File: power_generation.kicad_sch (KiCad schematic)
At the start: 0 parts

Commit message: Add 5V and 3.3V power generation
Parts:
- added C301, C307: 10 µF, Capacitor_SMD:C_0603_1608Metric, symbol Device:C
- added C302, C308: 0.1 µF, perfect_footprints:C_0402_1005Metric, symbol Device:C
- added C303: 3300 pF, symbol Device:C
- added C304, C305, C306, C310, C311, C312: 22 µF, symbol Device:C
- added C309: 3600 pF, symbol Device:C
- added D301, D302: 150060RS75000, LED_SMD:LED_0603_1608Metric, symbol Device:LED
- added J301, J302: 61300211121, Connector_PinHeader_2.54mm:PinHeader_2x01_P2.54mm_Vertical, symbol Connector_Generic:Conn_01x02
- added L301: 3.3 µH, symbol Device:L
- added L302: 2.7 µH, symbol Device:L
- added R301: 127 kΩ, perfect_footprints:R_0402_1005Metric, symbol Device:R
- added R302: 24 kΩ, perfect_footprints:R_0402_1005Metric, symbol Device:R
- added R303: 34.8 kΩ, perfect_footprints:R_0402_1005Metric, symbol Device:R
- added R304, R305: 100 kΩ, perfect_footprints:R_0402_1005Metric, symbol Device:R
- added R306: 23.7 kΩ, perfect_footprints:R_0402_1005Metric, symbol Device:R
- added R307: 215 kΩ, perfect_footprints:R_0402_1005Metric, symbol Device:R
- added R308: 68 kΩ, perfect_footprints:R_0402_1005Metric, symbol Device:R
- added R309: 1 kΩ, perfect_footprints:R_0402_1005Metric, symbol Device:R
- added R310, R311: 0 Ω, Resistor_SMD:R_0805_2012Metric, symbol Device:R
- added R312: 330 Ω, perfect_footprints:R_0402_1005Metric, symbol Device:R
- added U301, U302: AP64500SP-13, Package_SO:Diodes_SO-8EP, symbol Diodes Incorporated:AP64500
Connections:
- net V_3V3: now also C310.1, C311.1, C312.1, J302.1 (Pin_1), L302.2, R307.1, R311.2
- net V_5V0: now also C304.1, C305.1, C306.1, J301.1 (Pin_1), L301.2, R301.1, R310.2
- net V_SYS: now also C301.1, C307.1, U301.2 (VIN), U301.3 (EN), U302.2 (VIN), U302.3 (EN)
- new net: J301.2 (Pin_2), R309.1, R310.1
- new net: C309.1, R306.2
- new net: D301.2 (A), R309.2
- new net: J302.2 (Pin_2), R311.1, R312.1
- new net: C303.1, R303.2
- new net: D302.2 (A), R312.2
- new net BST_V_3V3: C308.1, U302.1 (BST)
- new net BST_V_5V0: C302.1, U301.1 (BST)
- new net COMP_V_3V3: R306.1, U302.6 (COMP)
- new net COMP_V_5V0: R303.1, U301.6 (COMP)
- new net FB_V_3V3: R307.2, R308.1, U302.5 (FB)
- new net FB_V_5V0: R301.2, R302.1, U301.5 (FB)
- new net GND: C301.2, C303.2, C304.2, C305.2, C306.2, C307.2, C309.2, C310.2, C311.2, C312.2, D301.1 (K), D302.1 (K), R302.2, R304.2, R305.2, R308.2, U301.7 (GND), U302.7 (GND)
- new net RT_V_3V3: R305.1, U302.4 (RT/CLK)
- new net RT_V_5V0: R304.1, U301.4 (RT/CLK)
- new net SW_V_3V3: C308.2, L302.1, U302.8 (SW)
- new net SW_V_5V0: C302.2, L301.1, U301.8 (SW)
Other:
- note added: "C_{COMP}"
- note added: "R_{COMP}"
- note added: "R_{FBB}"
- note added: "R_{FBT}"
- note added: "R_{RT}"

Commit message: Add MPU power generation
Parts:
- added TP301, TP302: TestPoint, TestPoint:TestPoint_Pad_D1.0mm, symbol Connector:TestPoint
- U301: MPN (none) -> AP64500SP-13; Manufacturer Part Number AP64500SP-13 -> (none)
- U302: MPN (none) -> AP64500SP-13
- renumbered C307 to C302, C302 to C303, C303 to C304, C308 to C305, C309 to C306, C304 to C307, C310 to C308, C305 to C309, C311 to C310, C306 to C311, R304 to R301, R305 to R302, R306 to R304, R301 to R305, R302 to R306, R310 to R309, R309 to R310
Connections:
- net V_3V3: now also TP302.1
- net V_5V0: now also TP301.1
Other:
- added sheet Power generation MPU (power_generation_mpu.kicad_sch)

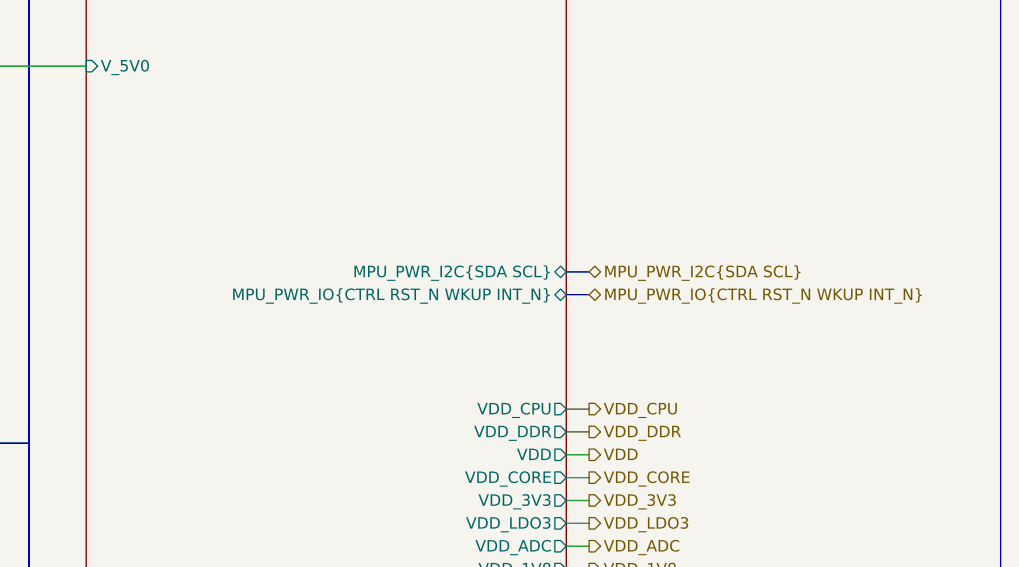
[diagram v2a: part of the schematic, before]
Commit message: Reorganize schema and add MPU
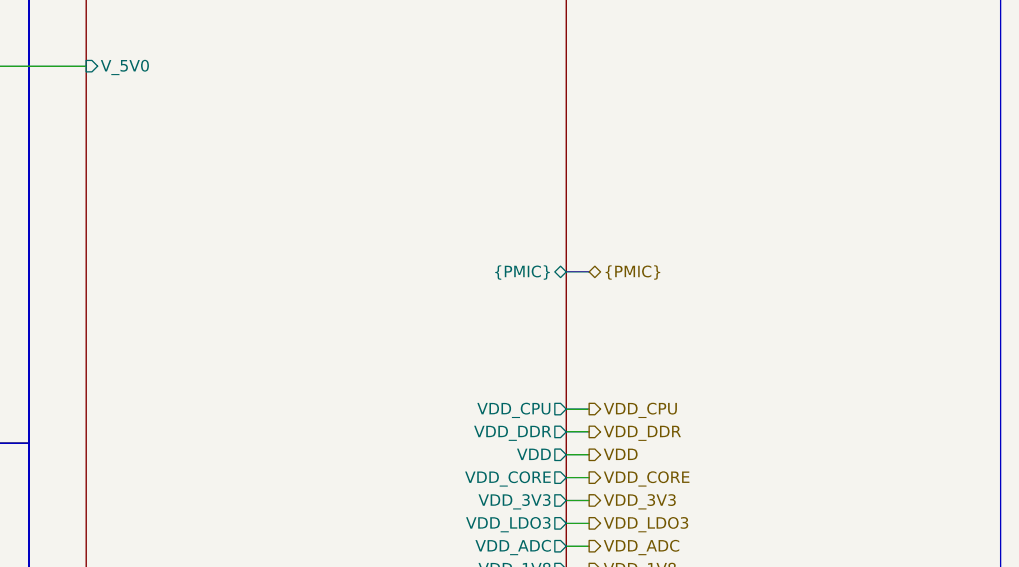
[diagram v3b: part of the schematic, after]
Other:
- sheet Power generation MPU ports: added {PMIC}; removed MPU_PWR_I2C{SDA SCL}, MPU_PWR_IO{CTRL RST_N WKUP INT_N}
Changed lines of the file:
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@@
 		)
 	)
-	(bus
-		(pts
-			(xy 358.14 129.54) (xy 360.68 129.54)
-		)
-		(stroke
-			(width 0)
-			(type default)
-		)
-	)
 	(wire
 		(pts
@@
 		)
 	)
-	(hierarchical_label "MPU_PWR_IO{CTRL RST_N WKUP INT_N}"
-		(shape bidirectional)
-		(at 360.68 129.54 0)
-		(effects
-			(font
-				(size 1.27 1.27)
-			)
-			(justify left)
-		)
-	)
 	(hierarchical_label "VDD_3V3"
 		(shape output)
@@
 		)
 	)
-	(hierarchical_label "MPU_PWR_I2C{SDA SCL}"
+	(hierarchical_label "{PMIC}"
 		(shape bidirectional)
 		(at 360.68 127 0)
@@
 			)
 		)
-		(pin "MPU_PWR_I2C{SDA SCL}" bidirectional
+		(pin "{PMIC}" bidirectional
 			(at 358.14 127 0)
 			(effects
 				(font
-					(size 1.27 1.27)
-				)
-				(justify right)
-			)
-		)
-		(pin "MPU_PWR_IO{CTRL RST_N WKUP INT_N}" bidirectional
-			(at 358.14 129.54 0)
-			(effects
-				(font

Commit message: Reorganize schema
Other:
- removed sheet Power generation MPU

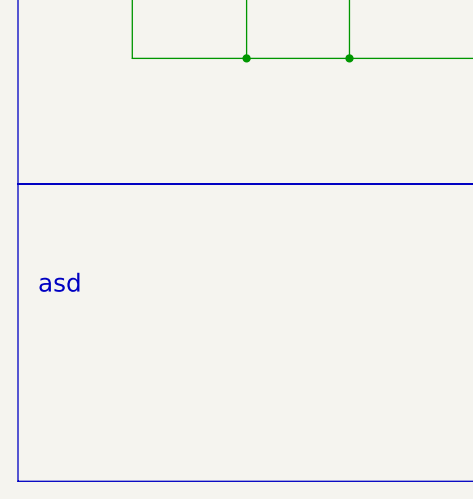
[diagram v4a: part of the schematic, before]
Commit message: Add MPU boot selection
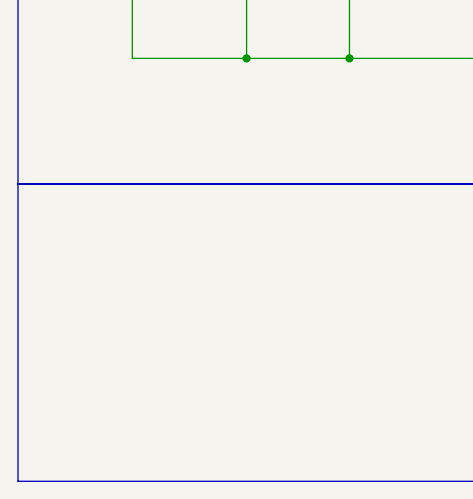
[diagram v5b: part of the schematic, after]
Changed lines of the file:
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@@
-		)
-	)
-	(text_box "asd"
-		(exclude_from_sim no)
-		(at 13.97 260.35 0)
-		(size 283.21 22.86)
-		(margins 0.9525 0.9525 0.9525 0.9525)
-		(stroke
-			(width -0.0001)
-			(type solid)
-		)
-		(fill
-			(type none)
-		)
-		(effects
-			(font
-				(size 2 2)
-			)
-			(justify left top)
 		)
 	)

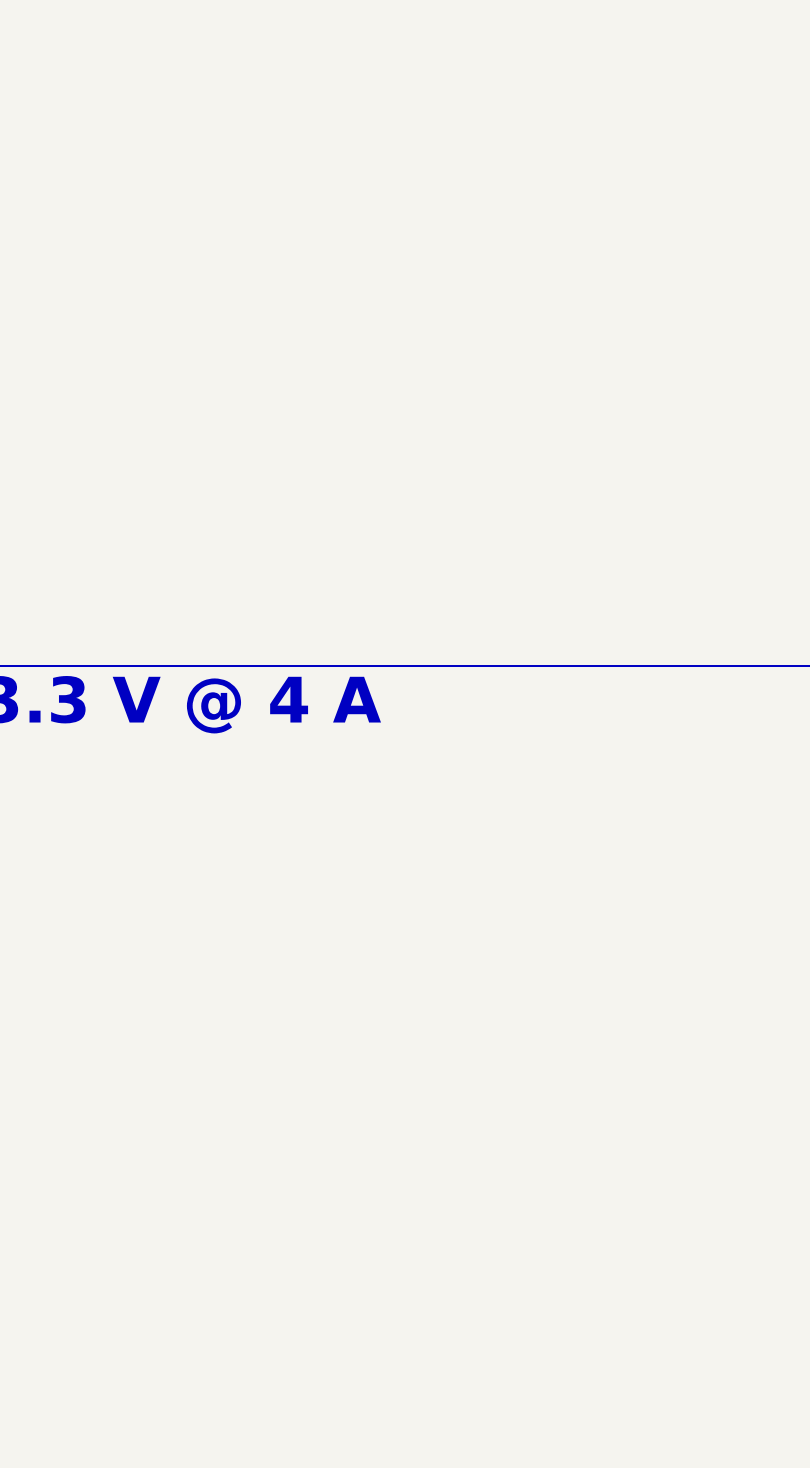
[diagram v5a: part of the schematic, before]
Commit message: Add series termination, refactor schematics
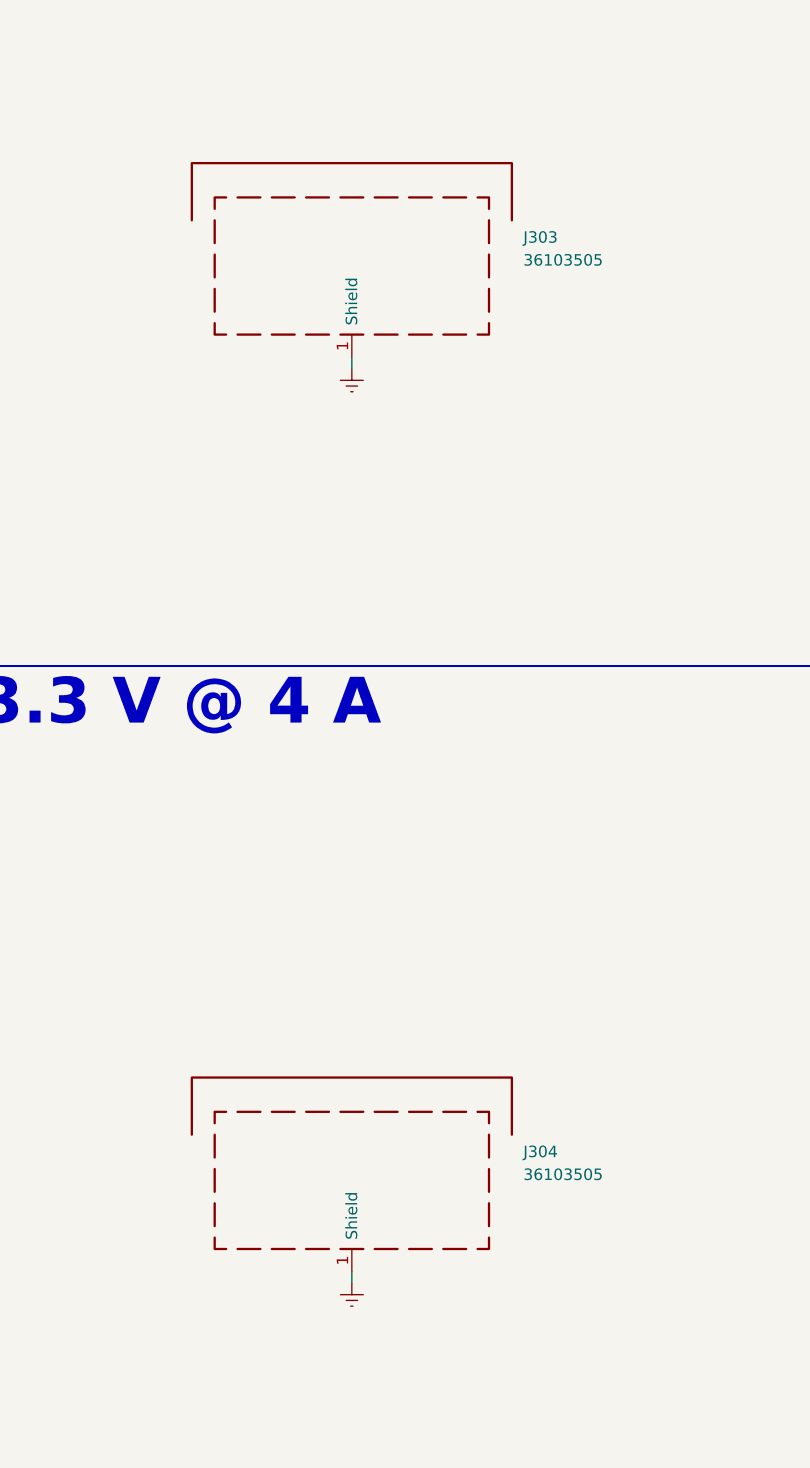
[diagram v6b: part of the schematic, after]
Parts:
- added J303, J304: 36103505, symbol Device:RFShield_TwoPieces
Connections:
- net GND: now also J303.1 (Shield), J304.1 (Shield)

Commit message: Refactor symbol properties
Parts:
- C301, C302: DigiKey Part Number 490-13248-1-ND -> (none)
- C303, C305: DigiKey Part Number 490-10700-1-ND -> (none)
- D301, D302: DigiKey Part Number 732-4978-1-ND -> (none)
- J301, J302: DigiKey Part Number 732-5315-ND -> (none)
- R301, R302, R310, R312: DigiKey Part Number 732-560112110019CT-ND -> (none)
- R305, R307: DigiKey Part Number 732-560112110195CT-ND -> (none)
- R306, R308: DigiKey Part Number 732-560112110178CT-ND -> (none)
- R309, R311: DigiKey Part Number 732-560112120002CT-ND -> (none)
- U302: Manufacturer Part Number AP64500SP-13 -> (none)

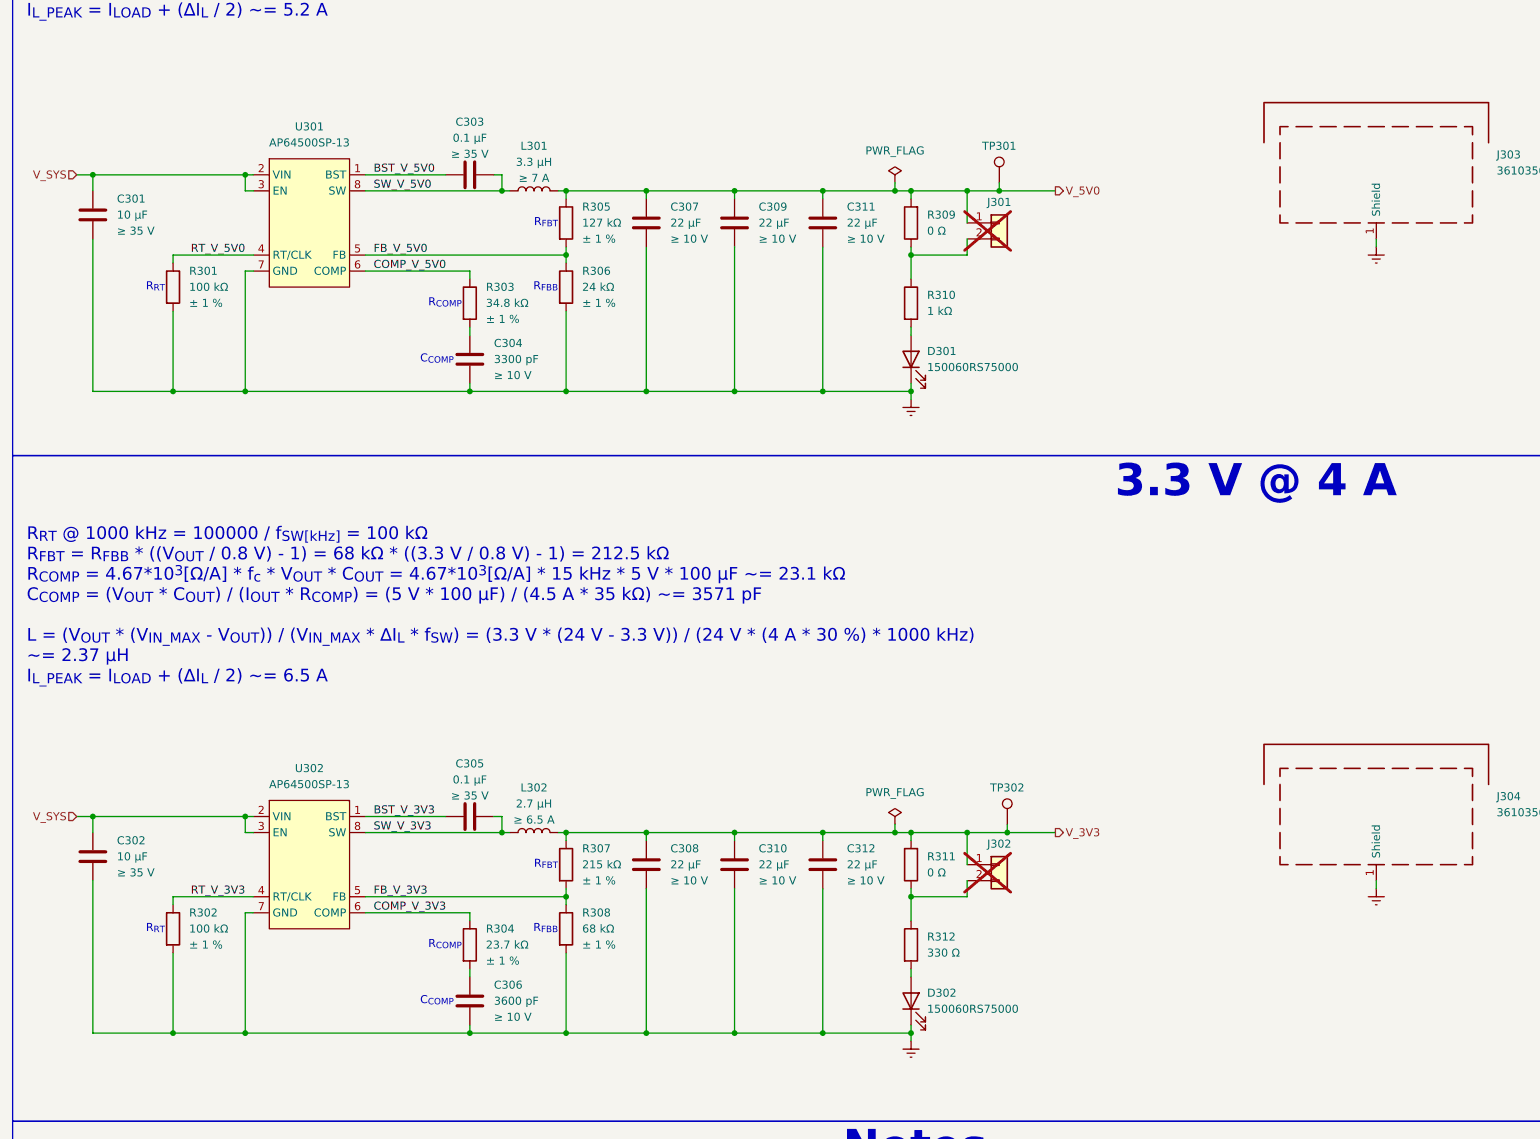
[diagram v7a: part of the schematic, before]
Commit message: Refactor power generation
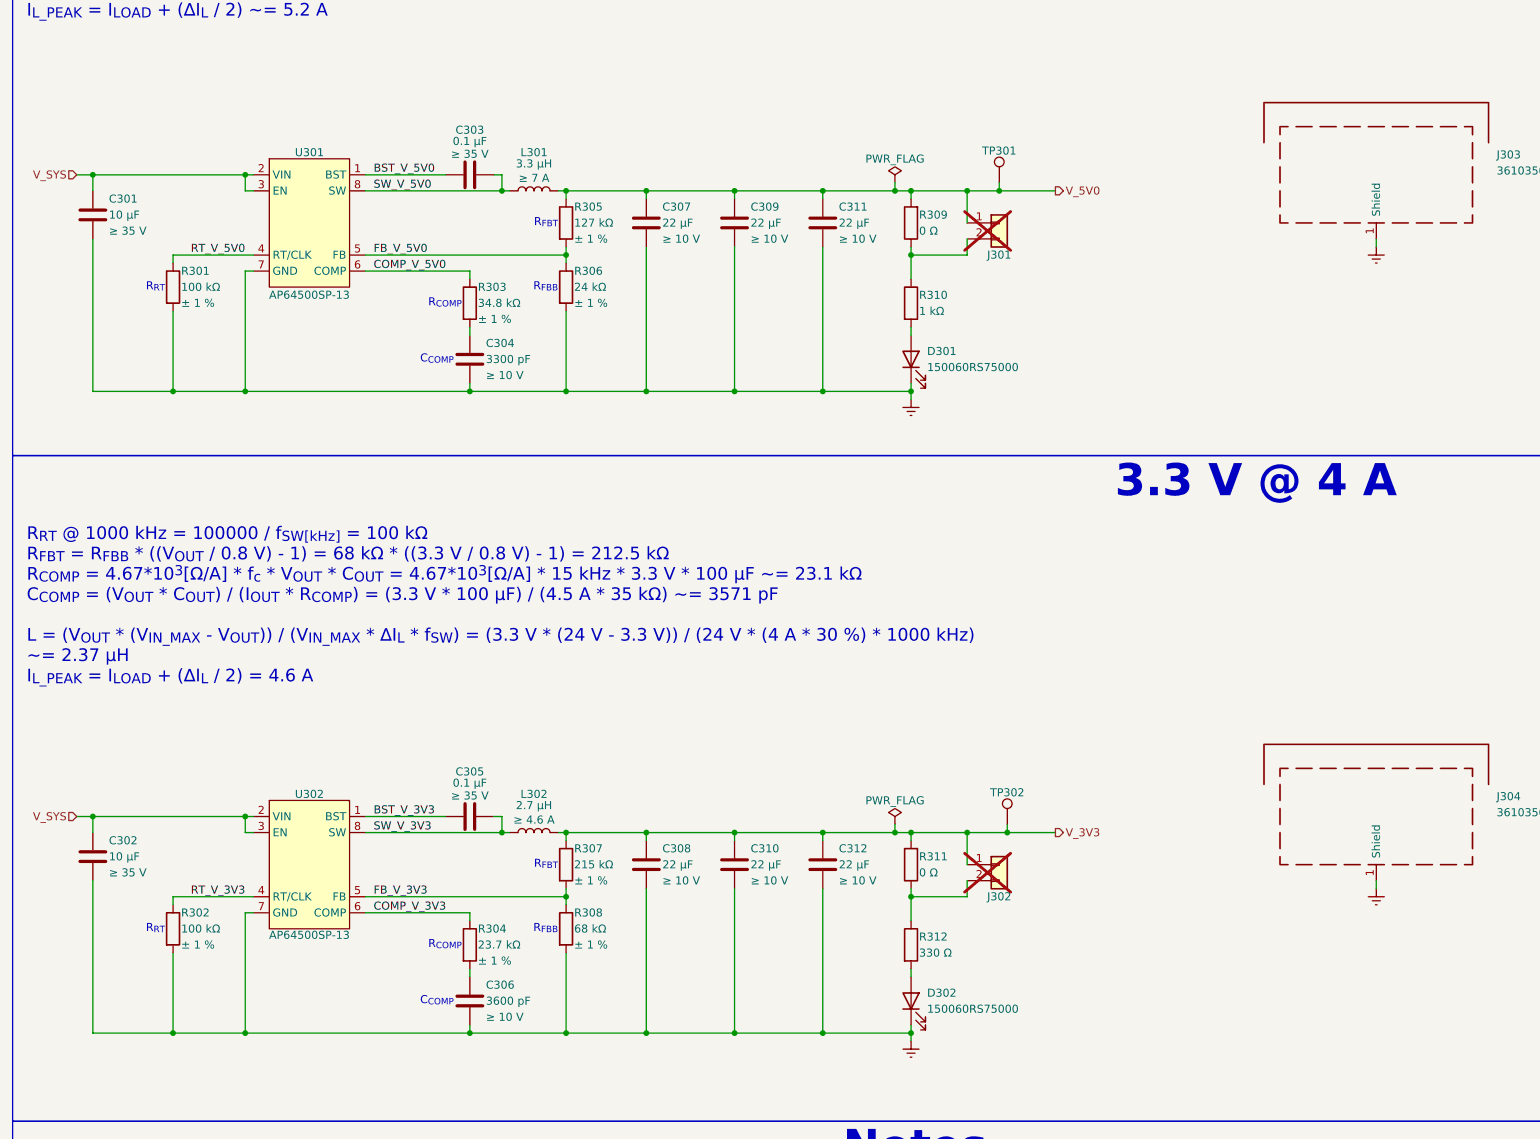
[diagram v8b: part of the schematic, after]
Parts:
- L302: Current rating ≥ 6.5 A -> ≥ 4.6 A
